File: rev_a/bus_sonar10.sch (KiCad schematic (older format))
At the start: 63 parts, among them J1 POWER_SELECT, J2 TERMINATE_JUMPER, SW1 MJTP1243, U1 LM2940, U2 LTV-826, U3 LTV-826, U4 LTV-826, U5 754410, U6 LM2940, U7 74HCT08, U8 MCP2562, U9 ATMEGA328_DIP28, X1 CRYSTAL

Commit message: Finnished laying out Rev. A
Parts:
- removed C1, C3: 22uF, symbol C_VERT
- removed C2, C4: .1uF, symbol C_VERT
- removed J1: POWER_SELECT, symbol POWER_SELECT
- removed N3, N4: ENCODER_CONNECTOR, symbol ENCODER_CONNECTOR
- removed N5, N6: MOTOR_CONNECTOR, symbol MOTOR_CONNECTOR
- removed N7, N8: HC_SR04_CONNECTOR, symbol HC_SR04_CONNECTOR
- removed R1: .47, symbol R_HORIZ
- removed R10, R11, R12, R13, R8, R9: 10K, symbol R_VERT
- removed R18, R21: 33K, symbol R_VERT
- removed R2, R3, R4, R5, R6, R7: 470, symbol R_HORIZ
- removed U1: LM2940, symbol VOLTAGE_REGULATOR
- removed U2, U3, U4: LTV-826, symbol OPTO_ISOLATOR
- removed U5: 754410, symbol 754410
- added C11: .1uF, symbol C_VERT
- added N3, N4: 302-S401, symbol SONAR_40_CONNECTOR
- added U5: 74HCT32, symbol 74LS32
- C10: value .1uF -> 1uF
- R4: renamed from R17; value 22K -> 100K
- R5: renamed from R20; value 22K -> 100K
- renumbered C5 to C1, C6 to C2, C7 to C3, C8 to C4, C9 to C5, C11 to C6, C12 to C7, C13 to C8, C14 to C9, J2 to J1, R14 to R1, R15 to R2, R16 to R3, R19 to R6, R22 to R7, U7 to U1, U6 to U2, U8 to U3, U9 to U4
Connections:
- net +5V: now also C11.1, N3.15 (VCC), N3.23 (VCC), N3.31 (VCC), N3.39 (VCC), N3.7 (VCC), N4.15 (VCC), N4.23 (VCC), N4.31 (VCC), N4.39 (VCC), N4.7 (VCC), U5.14 (VCC), U5.14 (VCC), U5.14 (VCC), U5.14 (VCC)
- net D10: now also N4.19 (ECHO3)
- net D11: now also U5.11
- net D12: now also N3.29 (TRIG4)
- net D13: now also N3.13 (TRIG2)
- net D2: now also N4.37 (TRIG5)
- net D3: now also U5.8
- net D4: now also N4.29 (TRIG4)
- net D5: now also U5.6
- net D6: now also N3.19 (ECHO3)
- net D7: now also N4.21 (TRIG3)
- net D8: now also N3.37 (TRIG5)
- net D9: now also U5.3
- net GND: now also C11.2, N3.1 (GND), N3.10 (GND), N3.12 (GND), N3.14 (GND), N3.16 (GND), N3.17 (GND), N3.18 (GND), N3.2 (GND), N3.20 (GND), N3.22 (GND), N3.24 (GND), N3.25 (GND), N3.26 (GND), N3.28 (GND), N3.30 (GND), N3.32 (GND), N3.33 (GND), N3.34 (GND), N3.36 (GND), N3.38 (GND), N3.4 (GND), N3.40 (GND), N3.6 (GND), N3.8 (GND), N3.9 (GND), N4.1 (GND), N4.10 (GND), N4.12 (GND), N4.14 (GND), N4.16 (GND), N4.17 (GND), N4.18 (GND), N4.2 (GND), N4.20 (GND), N4.22 (GND), N4.24 (GND), N4.25 (GND), N4.26 (GND), N4.28 (GND), N4.30 (GND), N4.32 (GND), N4.33 (GND), N4.34 (GND), N4.36 (GND), N4.38 (GND), N4.4 (GND), N4.40 (GND), N4.6 (GND), N4.8 (GND), N4.9 (GND), U5.7 (GND), U5.7 (GND), U5.7 (GND), U5.7 (GND)
- net at U4.25 (PC2/ADC2): now also N4.13 (TRIG2)
- net at U4.26 (PC3/ADC3): now also N4.5 (TRIG1)
- net A0: no longer names the net of U4.23 (PC0/ADC0)
- net A0: now also N3.21 (TRIG3)
- net A1: no longer names the net of U4.24 (PC1/ADC1)
- net A1: now also N3.5 (TRIG1)
- net BGND: no longer names the net of N1.7 (BGND1), N1.8 (BGND2)
- net BPWR: no longer names the net of N1.10 (BPWR2), N1.9 (BPWR1)
- new net: N3.11 (ECHO2), U5.2
- new net: N3.27 (ECHO4), U5.4
- new net: N3.3 (ECHO1), U5.1
- new net: N3.35 (ECHO5), U5.5
- new net: N4.11 (ECHO2), U5.13
- new net: N4.27 (ECHO4), U5.9
- new net: N4.3 (ECHO1), U5.12
- new net: N4.35 (ECHO5), U5.10
- no-connect marks 8 -> 6
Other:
- note removed: "+"
- note removed: "Electrically Isolated"
- moved on the sheet: C1, C3, C9, G1, H1, H2, H3, H4, U1A, U4, X1

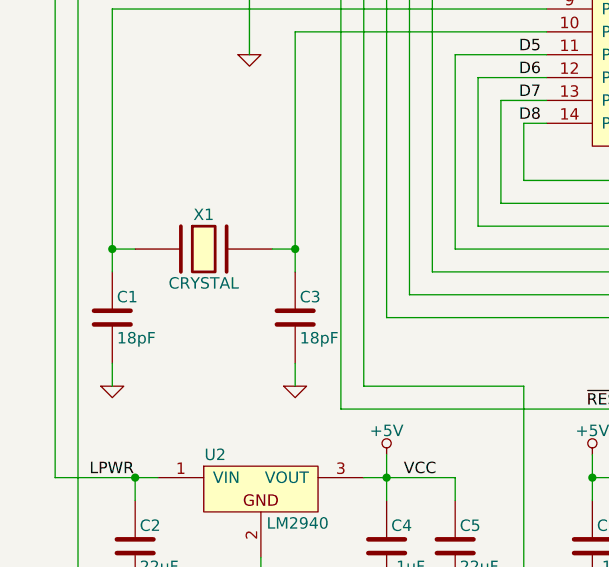
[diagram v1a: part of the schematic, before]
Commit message: CRYSTAL=>16MHz
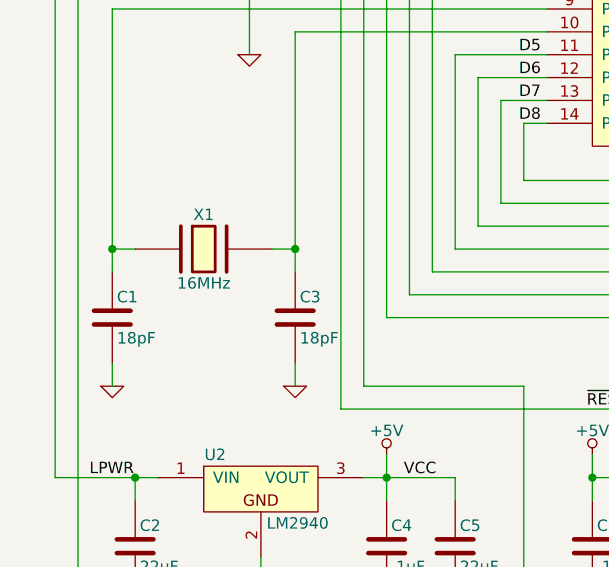
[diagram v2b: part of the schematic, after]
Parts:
- X1: value CRYSTAL -> 16MHz
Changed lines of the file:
@@
 P 1300 4450
 F 0 "X1" H 1300 4600 50  0000 C CNN
-F 1 "CRYSTAL" H 1300 4300 50  0000 C CNN
+F 1 "16MHz" H 1300 4300 50  0000 C CNN
 F 2 "" H 1300 4450 60  0000 C CNN
 F 3 "" H 1300 4450 60  0000 C CNN
